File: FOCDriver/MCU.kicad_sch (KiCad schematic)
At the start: 73 parts, among them J10 Conn_01x04, J11 Conn_01x04, J4 Conn_02x05_Odd_Even, J9 Conn_01x04, M1 Fan_Tacho_PWM, Q1 NMOS, SW1 SW_Push, SW2 SW_Push, SW3 SW_Push, U1 STM32H725IGTx, U11 MCP1501-25xSN, U12 TMP1075DSG, U3 24LC64, Y1 Crystal_GND24

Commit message: Update
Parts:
- D3, D4, D5, D6: value LED -> APT2012SYCK; MPN (none) -> APT2012SYCK
- Q1: value NMOS -> 2N7002
- R69, R70, R74, R75: value 100 -> 100R
- RN1: value R_Pack04 -> EXB-38V102JV
- RN2, RN3, RN4, RN5: value R_Pack04 -> EXB-N8N220JX
- U11: value MCP1501-25xSN -> MCP1501-25E/SN; MPN (none) -> MCP1501-25E/SN
- Y1: value Crystal_GND24 -> ECS-250-18-33-JGN-TR3; MPN (none) -> ECS-250-18-33-JGN-TR3
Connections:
- net TIM2_CH1: no longer names the net of U1.50 (PA5)
- no-connect marks 1 -> 3
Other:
- note added: "1kR"
- note added: "22R"
- note added: "24MHz nominal"
- note added: "4-pin PC fan"
- note added: "Button, LEDs"
- note added: "EEPROM (STM32 Soft I2C)"
- note added: "I2C grove (STM32 I2C4)"
- note added: "PCB Cooling Fan"
- note added: "PCB temp Ch2 (STM32 Soft I2C)"
- note added: "SPI bus LCD (STM32 SPI1)"
- note added: "STM32 UART3"
- note added: "STM32 UART8"
- note added: "SWD"
- moved on the sheet: C33, C63, D3, D4, D5, D6, J10, J11, J4, J9, JP1, M1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

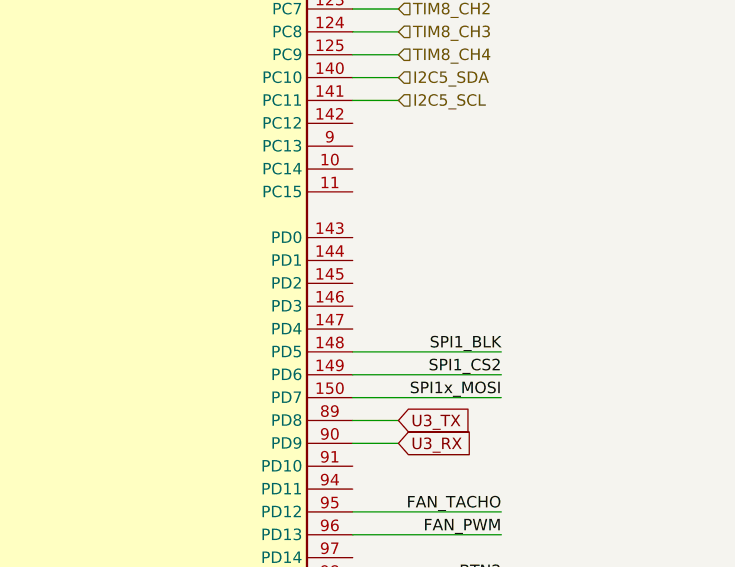
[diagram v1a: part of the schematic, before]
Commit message: Untented vias for DRVOFF signal Added unallocated IOs for DRVOFF potentially
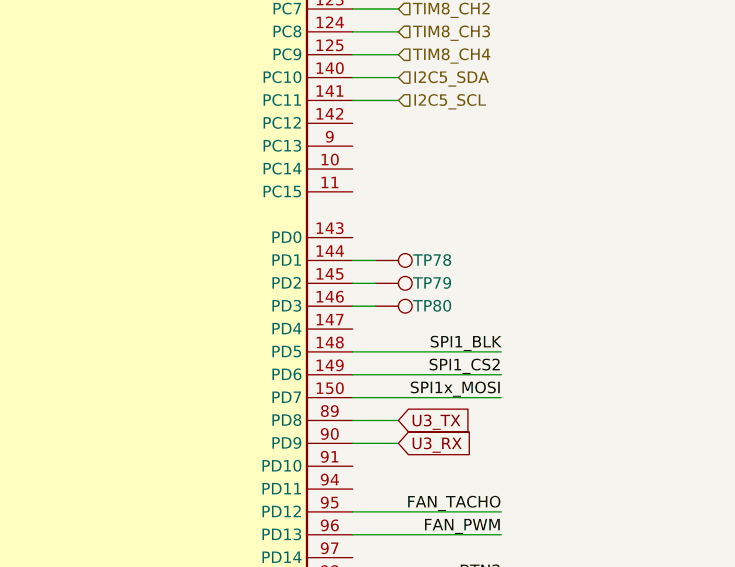
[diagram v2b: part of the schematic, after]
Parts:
- added TP78, TP79, TP80: TestPoint, Footprints:TP_0.6mm, symbol Connector:TestPoint
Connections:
- net at U1.144 (PD1): now also TP78.1
- net at U1.145 (PD2): now also TP79.1
- net at U1.146 (PD3): now also TP80.1
